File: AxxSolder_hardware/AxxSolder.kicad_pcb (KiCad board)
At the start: 2 copper layers, 39 x 82.5 mm, 136 parts, among them IC1 TLV76733DRVR, IC2 OPA2387DSGT, IC3 LMR54406DBVR, IC4 STM32G431CBT6, IC5 TPD4E1U06DBVR, IC6 STUSB4500QTR, IC7 MAX16171ATA_VY+T, IC8 LTC4440AHMS8E, J1 USB4110-GF-A, J2 691243110009, J3 TSW-102-07-T-S, J4 61300611821, J5 TSW-102-07-T-S, J6 TSW-102-07-T-S, Q1 STL9P3LLH6, Q2 STL10N3LLH5, Q3 2N7002NXAKR, U2 PEC11J-9215F-S0015, U3 BSC014N04LS

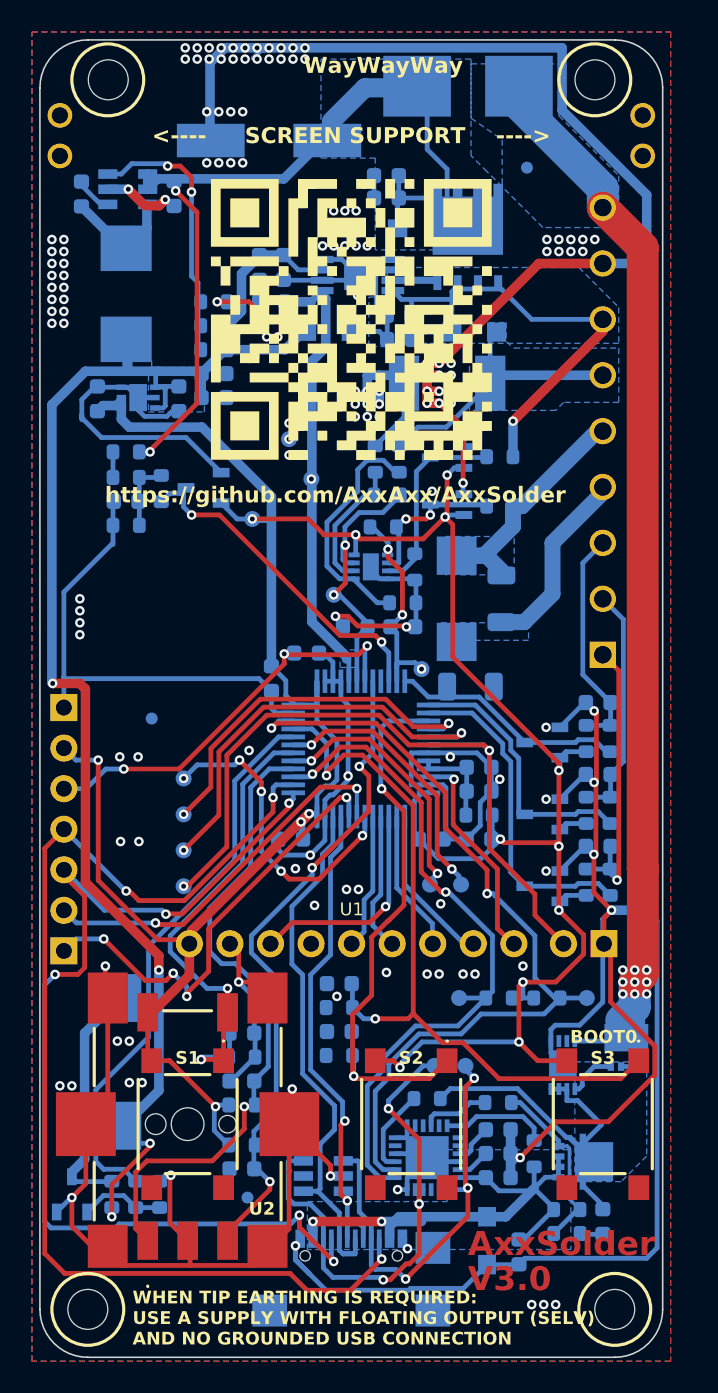
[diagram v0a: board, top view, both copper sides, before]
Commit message: update design with I_LEAK current sensor
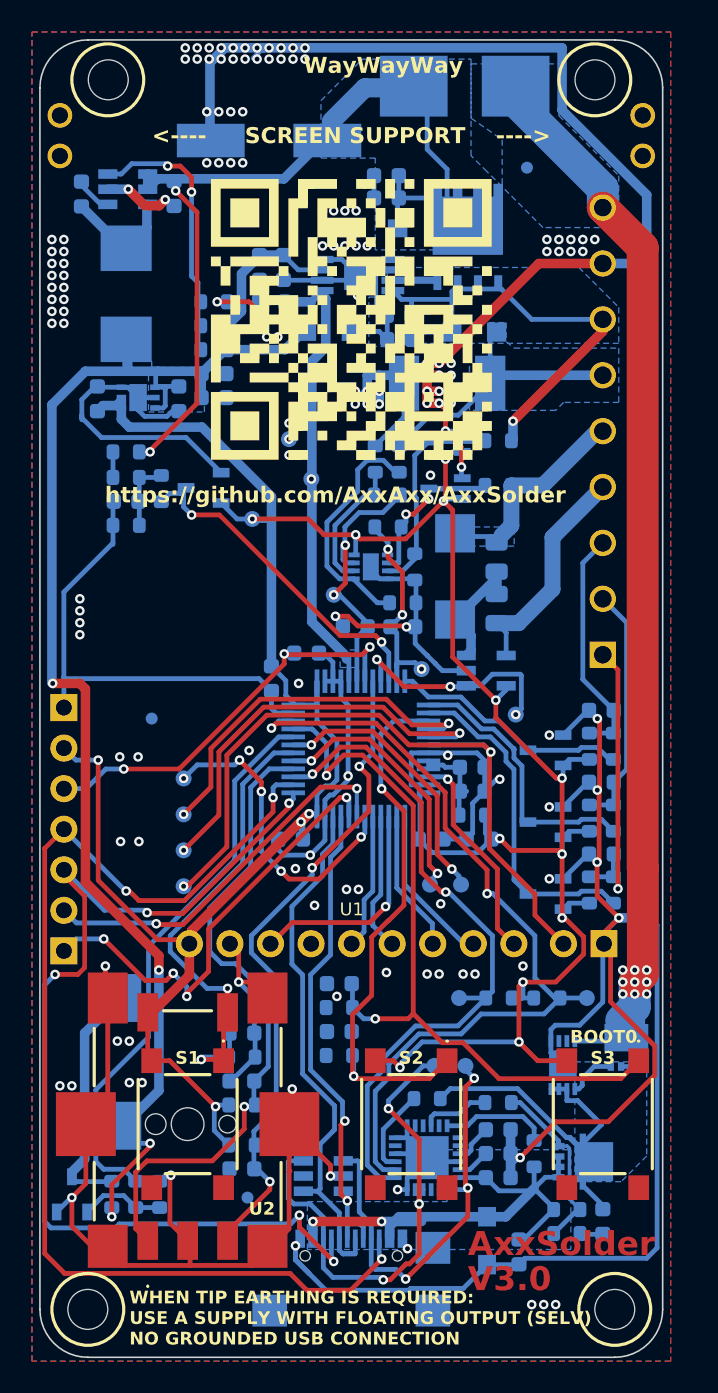
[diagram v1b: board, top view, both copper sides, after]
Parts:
- removed R16, R43: 1M, Resistor_SMD:R_1206_3216Metric
- added IC9: INA180A4IDBVT, footprints:SOT95P280X145-5N, B.Cu at (188.9, 107.0)
- added R44: 1M, Resistor_SMD:R_0805_2012Metric, B.Cu at (189.6, 99.9)
- added R45: 1, Resistor_SMD:R_0805_2012Metric, B.Cu at (189.6, 103.1)
- added TP9: Current_TP, TestPoint:TestPoint_Pad_D1.0mm, B.Cu at (190.8, 109.8)
- moved F2 1.40 mm to (187.0, 101.1)
- moved R5 1.30 mm to (189.7, 95.4)
- moved R1 1.00 mm to (189.7, 92.6)
- moved D1 1.00 mm to (186.4, 92.7)
- moved D2 1.00 mm to (186.4, 95.6)
- moved C25 0.52 mm to (196.2, 118.5)
- moved C26 0.52 mm to (196.2, 114.0)
- moved C27 0.52 mm to (196.2, 109.5)
- moved D5 0.52 mm to (192.7, 112.0)
- moved D6 0.52 mm to (192.7, 116.5)
- moved D8 0.52 mm to (192.7, 121.0)
- moved R18 0.52 mm to (195.4, 120.7)
- moved R19 0.52 mm to (195.4, 116.2)
- moved R20 0.52 mm to (195.4, 111.7)
- moved R22 0.52 mm to (196.9, 111.7)
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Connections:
- F2 pad 1: Earth -> Net-(IC9-IN+)
- IC4 pad 9: unconnected-(IC4-PA1-Pad9) -> /I_LEAK
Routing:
- net /I_LEAK: track 0.00 -> 14.3 mm, vias 0 -> 3
- net Net-(IC9-IN+): track 0.00 -> 9.07 mm
- net +3.3V: track 196.8 -> 199.9 mm, vias 15 -> 16
- net Earth: track 11.8 -> 14.5 mm
- net /GREEN: track 15.7 -> 13.2 mm
- net Net-(IC2A-+): track 12.3 -> 13.4 mm
- net GND: track 449.0 -> 447.9 mm, vias 151 -> 149
- net /RED: track 33.3 -> 32.4 mm
- net /S_sense: track 18.5 -> 19.2 mm
- net /H_sense1: track 14.2 -> 14.8 mm
- net /H_sense2: track 14.8 -> 15.4 mm
- net /Handle_inp2: track 17.0 -> 17.5 mm
- removed copper zone on B.Cu, net Earth
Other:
- board text added: "STAND"
- board text added: "WHEN TIP EARTHING IS REQUIRED: USE A SUPPLY WITH FLOATING OUTPUT (SELV) NO GROUNDED USB CONNECTION"
- board text removed: "STND"
- board text removed: "VDD"
- board text removed: "WHEN TIP EARTHING IS REQUIRED: USE A SUPPLY WITH FLOATING OUTPUT (SELV) AND NO GROUNDED USB CONNECTION"

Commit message: Final changes after sending AxxSolder 3.0 for manufacturing
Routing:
- net unconnected-(J1-SHIELD-PadS1): track 0.00 -> 10.2 mm
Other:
- board text added: "WHEN TIP GROUNDING IS REQUIRED: USE A SUPPLY WITH FLOATING OUTPUT (SELV) NO GROUNDED USB CONNECTION"
- board text removed: "WHEN TIP EARTHING IS REQUIRED: USE A SUPPLY WITH FLOATING OUTPUT (SELV) NO GROUNDED USB CONNECTION"
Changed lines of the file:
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@@
     (pad "2" thru_hole oval (at 0 -2.54 90) (size 1.7 1.7) (drill 1) (layers "*.Cu" "*.Mask")
       (net 57 "/USR4") (pinfunction "Pin_2") (pintype "passive"))
-    (model "${KICAD6_3DMODEL_DIR}/Connector_PinHeader_2.54mm.3dshapes/PinHeader_1x02_P2.54mm_Vertical.wrl"
+    (model "${KICAD6_3DMODEL_DIR}/Connector_PinHeader_2.54mm.3dshapes/PinHeader_1x02_P2.54mm_Vertical.wrl" hide
       (offset (xyz 0 0 0))
       (scale (xyz 1 1 1))
@@
     (pad "6" thru_hole oval (at 12.7 0 180) (size 1.7 1.7) (drill 1) (layers "*.Cu" "*.Mask")
       (net 59 "/USART_TX") (pinfunction "Pin_6") (pintype "passive"))
-    (model "${KICAD7_3DMODEL_DIR}/Connector_PinSocket_2.54mm.3dshapes/PinSocket_1x06_P2.54mm_Vertical.step"
+    (model "${KICAD7_3DMODEL_DIR}/Connector_PinSocket_2.54mm.3dshapes/PinSocket_1x06_P2.54mm_Vertical.step" hide
       (offset (xyz 0 0 0))
       (scale (xyz 1 1 1))
@@
     (fp_line (start 1 0.625) (end 1 -0.625)
       (stroke (width 0.1) (type solid)) (layer "B.Fab"))
-    (pad "1" smd roundrect (at -0.9125 0 90) (size 1.025 1.4) (layers "B.Cu" "B.Paste" "B.Mask") (roundrect_rratio 0.243902)
+    (pad "1" smd roundrect (at -0.9125 0 90) (size 1.025 1.4) (layers "B.Cu" "B.Paste" "B.Mask") (roundrect_rratio 0.243902439)
       (net 63 "Earth") (pintype "passive"))
-    (pad "2" smd roundrect (at 0.9125 0 90) (size 1.025 1.4) (layers "B.Cu" "B.Paste" "B.Mask") (roundrect_rratio 0.243902)
+    (pad "2" smd roundrect (at 0.9125 0 90) (size 1.025 1.4) (layers "B.Cu" "B.Paste" "B.Mask") (roundrect_rratio 0.243902439)
       (net 82 "Net-(IC9-IN+)") (pintype "passive"))
     (model "${KICAD6_3DMODEL_DIR}/Resistor_SMD.3dshapes/R_0805_2012Metric.wrl"
@@
     (pad "1" thru_hole rect (at 0 0) (size 1.7 1.7) (drill 1) (layers "*.Cu" "*.Mask")
       (net 53 "/USART_RX") (pinfunction "1") (pintype "passive"))
-    (model "${KICAD6_3DMODEL_DIR}/Connector_PinSocket_2.54mm.3dshapes/PinSocket_1x01_P2.54mm_Vertical.wrl"
+    (model "${KICAD6_3DMODEL_DIR}/Connector_PinSocket_2.54mm.3dshapes/PinSocket_1x01_P2.54mm_Vertical.wrl" hide
       (offset (xyz 0 0 0))
       (scale (xyz 1 1 1))
@@
     (fp_line (start 1 0.625) (end 1 -0.625)
       (stroke (width 0.1) (type solid)) (layer "B.Fab"))
-    (pad "1" smd roundrect (at -0.9125 0 90) (size 1.025 1.4) (layers "B.Cu" "B.Paste" "B.Mask") (roundrect_rratio 0.243902)
+    (pad "1" smd roundrect (at -0.9125 0 90) (size 1.025 1.4) (layers "B.Cu" "B.Paste" "B.Mask") (roundrect_rratio 0.243902439)
       (net 82 "Net-(IC9-IN+)") (pintype "passive"))
-    (pad "2" smd roundrect (at 0.9125 0 90) (size 1.025 1.4) (layers "B.Cu" "B.Paste" "B.Mask") (roundrect_rratio 0.243902)
+    (pad "2" smd roundrect (at 0.9125 0 90) (size 1.025 1.4) (layers "B.Cu" "B.Paste" "B.Mask") (roundrect_rratio 0.243902439)
       (net 9 "/GREEN") (pintype "passive"))
     (model "${KICAD6_3DMODEL_DIR}/Resistor_SMD.3dshapes/R_0805_2012Metric.wrl"
@@
     (effects (font (size 0.8 0.8) (thickness 0.15) bold) (justify left bottom))
   )
-  (gr_text "WHEN TIP EARTHING IS REQUIRED:\nUSE A SUPPLY WITH FLOATING OUTPUT (SELV)\nNO GROUNDED USB CONNECTION" (at 166.6 149.3) (layer "F.SilkS")
+  (gr_text "WHEN TIP GROUNDING IS REQUIRED:\nUSE A SUPPLY WITH FLOATING OUTPUT (SELV)\nNO GROUNDED USB CONNECTION" (at 166.6 149.3) (layer "F.SilkS")
     (effects (font (size 0.8 0.8) (thickness 0.15) bold) (justify left bottom))
   )
@@
   (segment (start 187.29038 110.90962) (end 187.05 111.15) (width 0.3) (layer "B.Cu") (net 56))
   (segment (start 189.14712 118.14712) (end 192 121) (width 0.3) (layer "F.Cu") (net 57))
-  (segment (start 172.708274 112.291726) (end 172.708274 118.030031) (width 0.3) (layer "F.Cu") (net 57))
-  (segment (start 189.14712 112.185499) (end 189.14712 118.14712) (width 0.3) (layer "F.Cu") (net 57))
   (segment (start 184.107106 111.65) (end 182.241726 109.78462) (width 0.3) (layer "F.Cu") (net 57))
-  (segment (start 192 122.315) (end 193.785 124.1) (width 0.3) (layer "F.Cu") (net 57))
+  (segment (start 189.14712 112.16288) (end 189.14712 118.14712) (width 0.3) (layer "F.Cu") (net 57))
+  (segment (start 170.238305 120.5) (end 170 120.5) (width 0.3) (layer "F.Cu") (net 57))
   (segment (start 172.708274 118.030031) (end 170.238305 120.5) (width 0.3) (layer "F.Cu") (net 57))
+  (segment (start 172.708274 112.291726) (end 172.708274 118.030031) (width 0.3) (layer "F.Cu") (net 57))
+  (segment (start 192 122.315) (end 193.785 124.1) (width 0.3) (layer "F.Cu") (net 57))
   (segment (start 192 121) (end 192 122.315) (width 0.3) (layer "F.Cu") (net 57))
+  (segment (start 189.22712 112.08288) (end 188.79424 111.65) (width 0.3) (layer "F.Cu") (net 57))
+  (segment (start 189.22712 112.08288) (end 189.14712 112.16288) (width 0.3) (layer "F.Cu") (net 57))
   (segment (start 175.21538 109.78462) (end 172.708274 112.291726) (width 0.3) (layer "F.Cu") (net 57))
-  (segment (start 189.238429 112.09419) (end 189.14712 112.185499) (width 0.3) (layer "F.Cu") (net 57))
   (segment (start 182.241726 109.78462) (end 175.21538 109.78462) (width 0.3) (layer "F.Cu") (net 57))
-  (segment (start 189.238429 112.09419) (end 188.794239 111.65) (width 0.3) (layer "F.Cu") (net 57))
-  (segment (start 170.238305 120.5) (end 170 120.5) (width 0.3) (layer "F.Cu") (net 57))
-  (segment (start 188.794239 111.65) (end 184.107106 111.65) (width 0.3) (layer "F.Cu") (net 57))
+  (segment (start 188.79424 111.65) (end 184.107106 111.65) (width 0.3) (layer "F.Cu") (net 57))
   (via (at 170 120.5) (size 0.6) (drill 0.3) (layers "F.Cu" "B.Cu") (net 57))
-  (via (at 189.238429 112.09419) (size 0.6) (drill 0.3) (layers "F.Cu" "B.Cu") (net 57))
-  (segment (start 189.238429 112.09419) (end 188.794239 111.65) (width 0.3) (layer "B.Cu") (net 57))
-  (segment (start 188.794239 111.65) (end 185.338 111.65) (width 0.3) (layer "B.Cu") (net 57))
+  (via (at 189.22712 112.08288) (size 0.6) (drill 0.3) (layers "F.Cu" "B.Cu") (net 57))
+  (segment (start 188.79424 111.65) (end 185.338 111.65) (width 0.3) (layer "B.Cu") (net 57))
+  (segment (start 189.22712 112.08288) (end 188.79424 111.65) (width 0.3) (layer "B.Cu") (net 57))
   (segment (start 179.79474 104.8) (end 172.24474 97.25) (width 0.3) (layer "F.Cu") (net 58))
   (segment (start 182 104.8) (end 179.79474 104.8) (width 0.3) (layer "F.Cu") (net 58))
@@
   (segment (start 193.475 136.448748) (end 193.475 136.775) (width 0.3) (layer "B.Cu") (net 78))
   (segment (start 194.825 140.75) (end 194.16 140.085) (width 0.22) (layer "B.Cu") (net 78))
+  (segment (start 175.393 147.08) (end 185.467 147.08) (width 1.8) (layer "B.Cu") (net 80))
+  (segment (start 175.39 147.077) (end 175.393 147.08) (width 1.8) (layer "B.Cu") (net 80))
+  (segment (start 185.467 147.08) (end 185.537 147.15) (width 1.8) (layer "B.Cu") (net 80))
   (segment (start 182.1 106.3) (end 183.8 108) (width 0.3) (layer "F.Cu") (net 81))
   (segment (start 183.8 108) (end 186.7 108) (width 0.3) (layer "F.Cu") (net 81))

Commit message: Update to new fuse and add alternative buzzer
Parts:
- F1: value 0154007.DRL -> 0154007.DR
- R45: value 1 -> 560m
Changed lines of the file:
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@@
     (tags "resistor")
     (property "Assembly Comment" "")
-    (property "Manufacturer_Name" "")
-    (property "Manufacturer_Part_Number" "")
-    (property "Mouser Part Number" "")
+    (property "Manufacturer_Name" "Panasonic")
+    (property "Manufacturer_Part_Number" "ERJ-U6QJR56V")
+    (property "Mouser Part Number" "667-ERJ-U6QJR56V")
     (property "Sheetfile" "AxxSolder.kicad_sch")
     (property "Sheetname" "")
@@
         (effects (font (size 0.8 0.8) (thickness 0.15)) (justify mirror))
     )
-    (fp_text value "1" (at 0 -1.65 90) (layer "B.Fab")
+    (fp_text value "560m" (at 0 -1.65 90) (layer "B.Fab")
         (effects (font (size 1 1) (thickness 0.15)) (justify mirror))
     )
@@
     (property "Sheetname" "")
     (property "ki_description" "CONN USB 2.0 TYPE-C R/A SMT")
-    (attr through_hole)
     (fp_text reference "J1" (at 5.3 -2.95) (layer "B.SilkS")
         (effects (font (size 0.8 0.8) (thickness 0.15) bold) (justify mirror))
@@
     )
   )
-  (footprint "footprints:0154100DR" (layer "B.Cu")
-    (at 187.6 70.4)
-    (descr "0154.100DR-2")
-    (tags "Fuse")
-    (property "Height" "3.81")
-    (property "Manufacturer_Name" "LITTELFUSE")
-    (property "Manufacturer_Part_Number" "0154007.DRL")
-    (property "Mouser Part Number" "576-0154007.DRL")
-    (property "Mouser Price/Stock" "https://www.mouser.co.uk/ProductDetail/Littelfuse/0154007.DRL?qs=tQeA2zcAjvUgVHfTrPW0Hg%3D%3D")
-    (property "Sheetfile" "AxxSolder.kicad_sch")
-    (property "Sheetname" "")
-    (property "ki_description" "Fuse Chip Very Fast Acting 7A SMD Solder Pad 9.73 X 5.03 X 3.81mm T/R")
-    (attr smd)
-    (fp_text reference "F1" (at 4.6 3.3 180) (layer "B.SilkS")
-        (effects (font (size 0.8 0.8) (thickness 0.15) bold) (justify mirror))
-    )
-    (fp_text value "0154007.DRL" (at 0 -0.012 180) (layer "B.SilkS") hide
-        (effects (font (size 1.27 1.27) (thickness 0.254)) (justify mirror))
-    )
-    (fp_text user "${REFERENCE}" (at 0 -0.012 180) (layer "B.Fab")
-        (effects (font (size 1.27 1.27) (thickness 0.254)) (justify mirror))
-    )
-    (fp_line (start -4.865 -2.54) (end 4.865 -2.515)
-      (stroke (width 0.1) (type solid)) (layer "B.SilkS"))
-    (fp_line (start -4.865 2.515) (end 4.865 2.515)
-      (stroke (width 0.1) (type solid)) (layer "B.SilkS"))
-    (fp_line (start -6.31 -3.54) (end -6.31 3.515)
-      (stroke (width 0.1) (type solid)) (layer "B.CrtYd"))
-    (fp_line (start -6.31 3.515) (end 6.31 3.515)
-      (stroke (width 0.1) (type solid)) (layer "B.CrtYd"))
-    (fp_line (start 6.31 -3.54) (end -6.31 -3.54)
-      (stroke (width 0.1) (type solid)) (layer "B.CrtYd"))
-    (fp_line (start 6.31 3.515) (end 6.31 -3.54)
-      (stroke (width 0.1) (type solid)) (layer "B.CrtYd"))
-    (fp_line (start -4.865 -2.515) (end -4.865 2.515)
-      (stroke (width 0.2) (type solid)) (layer "B.Fab"))
-    (fp_line (start -4.865 2.515) (end 4.865 2.515)
-      (stroke (width 0.2) (type solid)) (layer "B.Fab"))
-    (fp_line (start 4.865 -2.515) (end -4.865 -2.515)
-      (stroke (width 0.2) (type solid)) (layer "B.Fab"))
-    (fp_line (start 4.865 2.515) (end 4.865 -2.515)
-      (stroke (width 0.2) (type solid)) (layer "B.Fab"))
-    (pad "1" smd rect (at -3.19 0 270) (size 3.81 4.24) (layers "B.Cu" "B.Paste" "B.Mask")
-      (net 48 "VDD") (pinfunction "1") (pintype "passive"))
-    (pad "2" smd rect (at 3.19 0 270) (size 3.81 4.24) (layers "B.Cu" "B.Paste" "B.Mask")
-      (net 26 "/VDD_IN") (pintype "passive"))
-    (model "${KIPRJMOD}/3rd-parties-libraries/3D-models/0154007.DRTL.stp"
-      (offset (xyz 0 0 0))
-      (scale (xyz 1 1 1))
-      (rotate (xyz 0 0 0))
-    )
-  )
   (footprint "Capacitor_SMD:C_0603_1608Metric" (layer "B.Cu")
     (at 191 143.4 90)
@@
     )
   )
+  (footprint "footprints:0154100DR" (layer "B.Cu")
+    (at 187.6 70.4)
+    (descr "0154.100DR-2")
+    (tags "Fuse")
+    (property "Height" "3.81")
+    (property "Manufacturer_Name" "LITTELFUSE")
+    (property "Manufacturer_Part_Number" "0154007.DR")
+    (property "Mouser Part Number" "576-0154007.DR")
+    (property "Sheetfile" "AxxSolder.kicad_sch")
+    (property "Sheetname" "")
+    (property "ki_description" "Fuse Chip Very Fast Acting 7A SMD Solder Pad 9.73 X 5.03 X 3.81mm T/R")
+    (attr smd)
+    (fp_text reference "F1" (at 4.69 3.34) (layer "B.SilkS")
+        (effects (font (size 0.8 0.8) (thickness 0.15) bold) (justify mirror))
+    )
+    (fp_text value "0154007.DR" (at 0 -0.012) (layer "B.SilkS") hide
+        (effects (font (size 1.27 1.27) (thickness 0.254)) (justify mirror))
+    )
+    (fp_text user "${REFERENCE}" (at 0 -0.012) (layer "B.Fab")
+        (effects (font (size 1.27 1.27) (thickness 0.254)) (justify mirror))
+    )
+    (fp_line (start -4.865 -2.54) (end 4.865 -2.515)
+      (stroke (width 0.1) (type solid)) (layer "B.SilkS"))
+    (fp_line (start -4.865 2.515) (end 4.865 2.515)
+      (stroke (width 0.1) (type solid)) (layer "B.SilkS"))
+    (fp_line (start -6.31 -3.54) (end -6.31 3.515)
+      (stroke (width 0.1) (type solid)) (layer "B.CrtYd"))
+    (fp_line (start -6.31 3.515) (end 6.31 3.515)
+      (stroke (width 0.1) (type solid)) (layer "B.CrtYd"))
+    (fp_line (start 6.31 -3.54) (end -6.31 -3.54)
+      (stroke (width 0.1) (type solid)) (layer "B.CrtYd"))
+    (fp_line (start 6.31 3.515) (end 6.31 -3.54)
+      (stroke (width 0.1) (type solid)) (layer "B.CrtYd"))
+    (fp_line (start -4.865 -2.515) (end -4.865 2.515)
+      (stroke (width 0.2) (type solid)) (layer "B.Fab"))
+    (fp_line (start -4.865 2.515) (end 4.865 2.515)
+      (stroke (width 0.2) (type solid)) (layer "B.Fab"))
+    (fp_line (start 4.865 -2.515) (end -4.865 -2.515)
+      (stroke (width 0.2) (type solid)) (layer "B.Fab"))
+    (fp_line (start 4.865 2.515) (end 4.865 -2.515)
+      (stroke (width 0.2) (type solid)) (layer "B.Fab"))
+    (pad "1" smd rect (at -3.19 0 270) (size 3.81 4.24) (layers "B.Cu" "B.Paste" "B.Mask")
+      (net 48 "VDD") (pinfunction "1") (pintype "passive"))
+    (pad "2" smd rect (at 3.19 0 270) (size 3.81 4.24) (layers "B.Cu" "B.Paste" "B.Mask")
+      (net 26 "/VDD_IN") (pintype "passive"))
+    (model "${KIPRJMOD}/3rd-parties-libraries/3D-models/0154007.DRTL.stp"
+      (offset (xyz 0 0 0))
+      (scale (xyz 1 1 1))
+      (rotate (xyz 0 0 0))
+    )
+  )
   (footprint "TestPoint:TestPoint_Pad_D1.0mm" (layer "B.Cu")
     (at 170 118.25 180)
@@
     (tags "resistor")
     (property "Assembly Comment" "")
-    (property "Manufacturer_Name" "")
-    (property "Manufacturer_Part_Number" "")
-    (property "Mouser Part Number" "")
+    (property "Manufacturer_Name" "Panasonic")
+    (property "Manufacturer_Part_Number" "ERJ-6GEYJ105V")
+    (property "Mouser Part Number" "667-ERJ-6GEYJ105V")
     (property "Sheetfile" "AxxSolder.kicad_sch")
     (property "Sheetname" "")
@@
     (fp_line (start 1 0.625) (end 1 -0.625)
       (stroke (width 0.1) (type solid)) (layer "B.Fab"))
-    (pad "1" smd roundrect (at -0.9125 0 90) (size 1.025 1.4) (layers "B.Cu" "B.Paste" "B.Mask") (roundrect_rratio 0.243902439)
+    (pad "1" smd roundrect (at -0.9125 0 90) (size 1.025 1.4) (layers "B.Cu" "B.Paste" "B.Mask") (roundrect_rratio 0.243902)
       (net 82 "Net-(IC9-IN+)") (pintype "passive"))
-    (pad "2" smd roundrect (at 0.9125 0 90) (size 1.025 1.4) (layers "B.Cu" "B.Paste" "B.Mask") (roundrect_rratio 0.243902439)
+    (pad "2" smd roundrect (at 0.9125 0 90) (size 1.025 1.4) (layers "B.Cu" "B.Paste" "B.Mask") (roundrect_rratio 0.243902)
       (net 9 "/GREEN") (pintype "passive"))
     (model "${KICAD6_3DMODEL_DIR}/Resistor_SMD.3dshapes/R_0805_2012Metric.wrl"

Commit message: update current sense resistor to 100m ohm from 560m ohm
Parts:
- R45: value 560m -> 100m
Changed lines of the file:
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@@
     (property "Assembly Comment" "")
     (property "Manufacturer_Name" "Panasonic")
-    (property "Manufacturer_Part_Number" "ERJ-U6QJR56V")
-    (property "Mouser Part Number" "667-ERJ-U6QJR56V")
+    (property "Manufacturer_Part_Number" "ERJ-6DSFR10V")
+    (property "Mouser Part Number" "667-ERJ-6DSFR10V")
     (property "Sheetfile" "AxxSolder.kicad_sch")
     (property "Sheetname" "")
@@
         (effects (font (size 0.8 0.8) (thickness 0.15)) (justify mirror))
     )
-    (fp_text value "560m" (at 0 -1.65 90) (layer "B.Fab")
+    (fp_text value "100m" (at 0 -1.65 90) (layer "B.Fab")
         (effects (font (size 1 1) (thickness 0.15)) (justify mirror))
     )
